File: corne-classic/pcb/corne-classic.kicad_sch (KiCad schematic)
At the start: 87 parts, among them J1 MJ-4PP-9, J2 OLED, J3 LED, P1 i2c-pin, P2 i2c-pin, SW1 SW_PUSH, SW10 SW_PUSH, SW11 SW_PUSH, SW12 SW_PUSH, SW13 SW_PUSH, SW14 SW_PUSH, SW15 SW_PUSH, SW16 SW_PUSH, SW17 SW_PUSH, SW18 SW_PUSH, SW19 SW_PUSH, SW2 SW_PUSH, SW20 SW_PUSH, SW21 SW_PUSH, SW3 SW_PUSH, SW4 SW_PUSH, SW5 SW_PUSH, SW6 SW_PUSH, SW7 SW_PUSH, SW8 SW_PUSH, SW9 SW_PUSH, U1 ProMicro

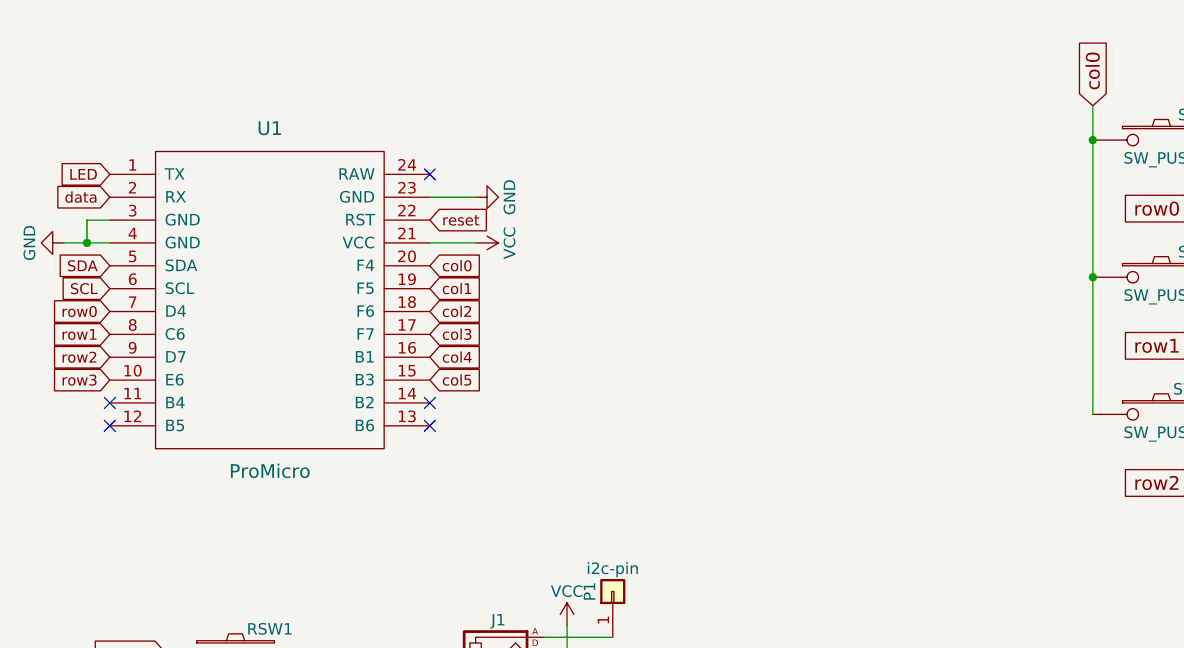
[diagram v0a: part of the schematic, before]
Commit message: Replaced Arduino by Esp32 TinyS3. Got a crash while rooting ...
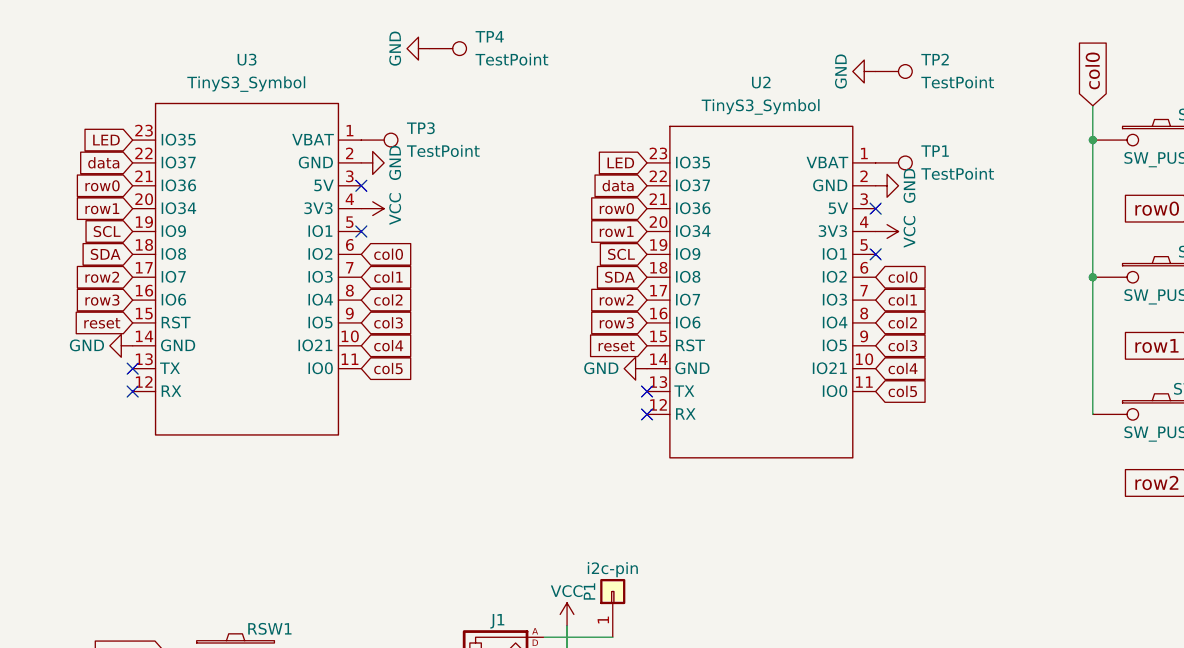
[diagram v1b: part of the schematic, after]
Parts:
- removed U1: ProMicro, kbd:ProMicro_v2, symbol corne-classic-rescue:ProMicro-kbd
- added TP1, TP2, TP3, TP4: TestPoint, TestPoint:TestPoint_Pad_D1.5mm, symbol Connector:TestPoint
- added U2, U3: TinyS3_Symbol, easyeda2kicad:TinyS3, symbol TinyS3:TinyS3_Symbol
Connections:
- net GND: now also TP2.1, TP4.1, U2.14 (GND), U2.2 (GND), U3.14 (GND), U3.2 (GND)
- net LED: now also U2.23 (IO35), U3.23 (IO35)
- net SCL: now also U2.19 (IO9), U3.19 (IO9)
- net SDA: now also U2.18 (IO8), U3.18 (IO8)
- net VCC: now also U2.4 (3V3), U3.4 (3V3)
- net col0: now also U2.6 (IO2), U3.6 (IO2)
- net col1: now also U2.7 (IO3), U3.7 (IO3)
- net col2: now also U2.8 (IO4), U3.8 (IO4)
- net col3: now also U2.9 (IO5), U3.9 (IO5)
- net col4: now also U2.10 (IO21), U3.10 (IO21)
- net col5: now also U2.11 (IO0), U3.11 (IO0)
- net data: now also U2.22 (IO37), U3.22 (IO37)
- net reset: now also U2.15 (RST), U3.15 (RST)
- net row0: now also U2.21 (IO36), U3.21 (IO36)
- net row1: now also U2.20 (IO34), U3.20 (IO34)
- net row2: now also U2.17 (IO7), U3.17 (IO7)
- net row3: now also U2.16 (IO6), U3.16 (IO6)
- new net: TP3.1, U3.1 (VBAT)
- new net: TP1.1, U2.1 (VBAT)
- no-connect marks 6 -> 9

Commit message: routing + prod files
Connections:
- net col0: now also U2.21 (IO36), U3.21 (IO36); no longer U2.6 (IO2), U3.6 (IO2)
- net col1: now also U2.20 (IO34), U3.20 (IO34); no longer U2.7 (IO3), U3.7 (IO3)
- net col2: now also U2.17 (IO7), U3.17 (IO7); no longer U2.8 (IO4), U3.8 (IO4)
- net col3: now also U2.7 (IO3), U3.7 (IO3); no longer U2.9 (IO5), U3.9 (IO5)
- net col4: now also U2.16 (IO6), U3.16 (IO6); no longer U2.10 (IO21), U3.10 (IO21)
- net col5: now also U2.8 (IO4), U3.8 (IO4); no longer U2.11 (IO0), U3.11 (IO0)
- net row0: now also U2.5 (IO1), U3.5 (IO1); no longer U2.21 (IO36), U3.21 (IO36)
- net row1: now also U2.6 (IO2), U3.6 (IO2); no longer U2.20 (IO34), U3.20 (IO34)
- net row2: now also U2.9 (IO5), U3.9 (IO5); no longer U2.17 (IO7), U3.17 (IO7)
- net row3: now also U2.10 (IO21), U3.10 (IO21); no longer U2.16 (IO6), U3.16 (IO6)
- net VBAT: now reaches TP3.1, U3.1 (VBAT)
- net VBAT: now also TP1.1, U2.1 (VBAT)
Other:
- moved on the sheet: TP1, TP3
